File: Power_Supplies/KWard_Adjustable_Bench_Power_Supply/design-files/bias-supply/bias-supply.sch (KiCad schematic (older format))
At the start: 23 parts, among them J1 168VAC input, J2 To C- meter, J3 To panel jacks, Q1 MJE5731, Q2 MJE5731, Q3 KSA1013

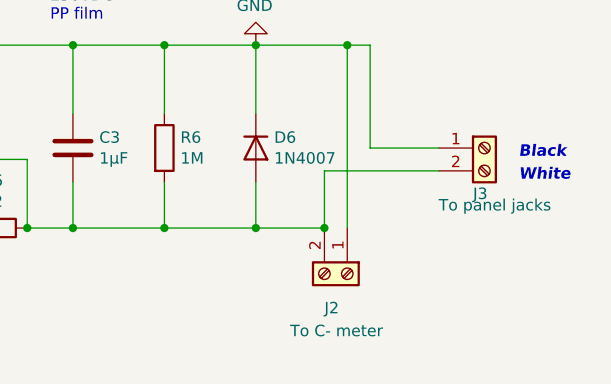
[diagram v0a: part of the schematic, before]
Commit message: Make the C- meter terminal a 3-position part, with a separate one for the GND reference.
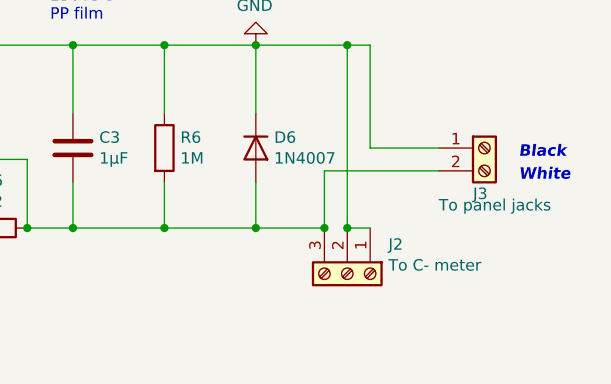
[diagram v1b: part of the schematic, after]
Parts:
- removed J2: To C- meter, TerminalBlock:TerminalBlock_bornier-2_P5.08mm, symbol Connector:Screw_Terminal_01x02
- added J2: To C- meter, TerminalBlock:TerminalBlock_bornier-3_P5.08mm, symbol Connector:Screw_Terminal_01x03
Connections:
- net GND: now also J2.1 (Pin_1), J2.2 (Pin_2)
- net at C3.2, D5.1 (K), D6.2 (A)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: now also J2.3 (Pin_3)
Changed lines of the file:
@@
 $EndComp
 Connection ~ 8200 3450
-$Comp
-L Connector:Screw_Terminal_01x02 J2
-U 1 1 64258EEA
-P 8600 4450
-F 0 "J2" V 8750 4350 50  0000 L CNN
-F 1 "To C- meter" V 8850 4200 50  0000 L CNN
-F 2 "TerminalBlock:TerminalBlock_bornier-2_P5.08mm" H 8600 4450 50  0001 C CNN
-F 3 "~" H 8600 4450 50  0001 C CNN
-	1    8600 4450
-	0    1    1    0
-$EndComp
 Wire Wire Line
 	8500 4250 8200 4250
@@
 Connection ~ 6100 3350
 Connection ~ 7400 3450
+$Comp
+L Connector:Screw_Terminal_01x03 J2
+U 1 1 61D5CFA2
+P 8600 4450
+F 0 "J2" V 8472 4630 50  0000 L CNN
+F 1 "To C- meter" V 8563 4630 50  0000 L CNN
+F 2 "TerminalBlock:TerminalBlock_bornier-3_P5.08mm" H 8600 4450 50  0001 C CNN
+F 3 "~" H 8600 4450 50  0001 C CNN
+	1    8600 4450
+	0    1    1    0
+$EndComp
+Wire Wire Line
+	8700 4250 8600 4250
+Connection ~ 8600 4250
 $EndSCHEMATC

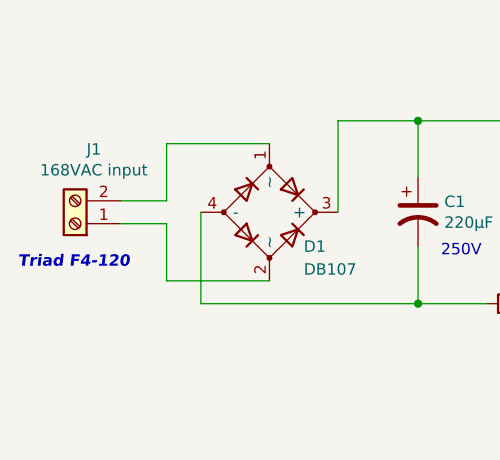
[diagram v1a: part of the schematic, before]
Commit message: Note that the bias supply is connected to the Main 120Vac.
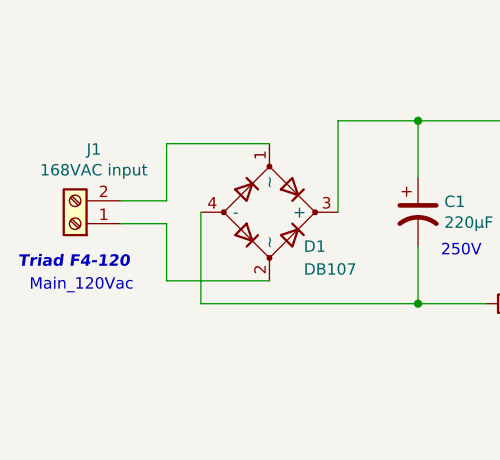
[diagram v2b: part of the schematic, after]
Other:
- note added: "Main_120Vac"
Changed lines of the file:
@@
 	8700 4250 8600 4250
 Connection ~ 8600 4250
+Text Notes 1550 4200 0    50   ~ 0
+Main_120Vac
 $EndSCHEMATC

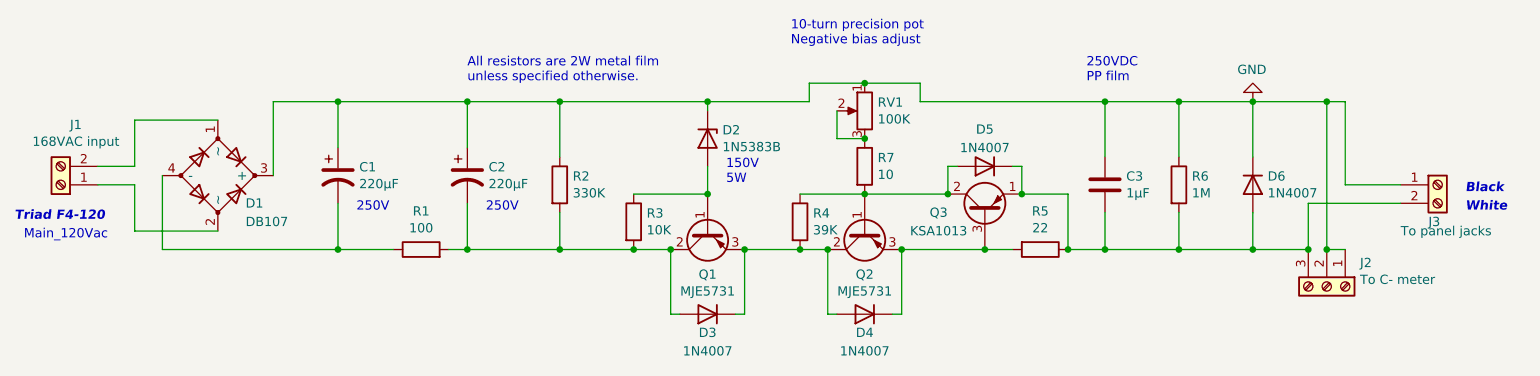
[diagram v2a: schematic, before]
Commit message: Correct AC input value label, add some part numbers, tweak some text.
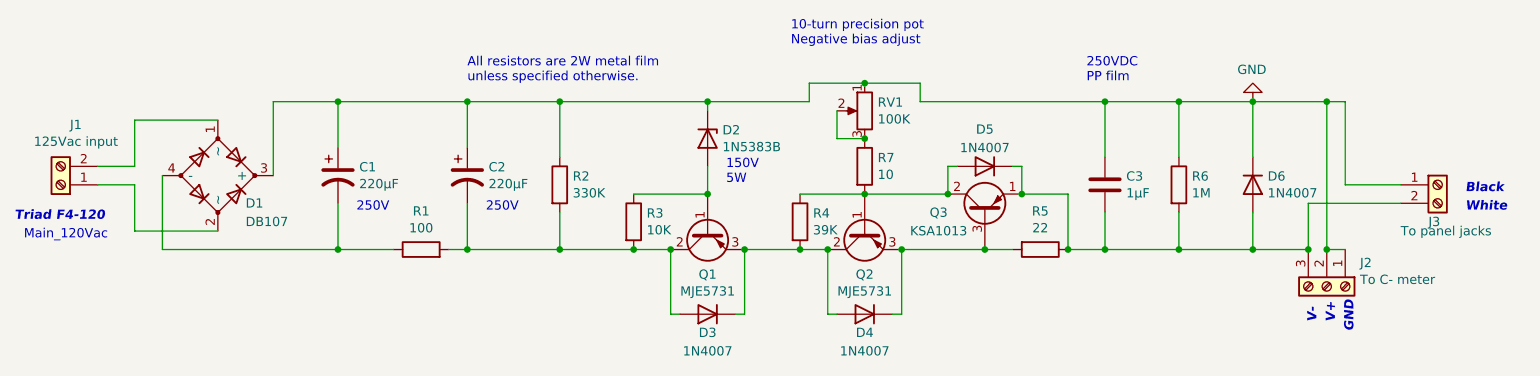
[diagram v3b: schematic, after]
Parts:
- D2: Mouser (none) -> 863-1N5383BG
- D6: Mouser (none) -> 621-1N4007G-T
- J1: value 168VAC input -> 125Vac input
- Q1, Q2: Mouser (none) -> 863-MJE5731G
- Q3: Mouser (none) -> 512-KSA1013YBU
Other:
- note added: "GND"
- note added: "V+"
- note added: "V-"
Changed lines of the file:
@@
 Sheet 1 1
 Title "KWard Bench PSU - Bias supply"
-Date ""
-Rev "0.1"
-Comp "Copyright (c) 2021 Jason R. Thorpe. See LICENSE."
+Date "2022-01-01"
+Rev "1.0"
+Comp "Copyright (c) 2017-2022 Kevin Ward and Jason R. Thorpe. See LICENSE."
 Comment1 ""
 Comment2 ""
@@
 P 1750 3900
 F 0 "J1" H 1668 3575 50  0000 C CNN
-F 1 "168VAC input" H 1668 3666 50  0000 C CNN
+F 1 "125Vac input" H 1668 3666 50  0000 C CNN
 F 2 "TerminalBlock:TerminalBlock_bornier-2_P5.08mm" H 1750 3900 50  0001 C CNN
 F 3 "~" H 1750 3900 50  0001 C CNN
@@
 F 2 "Diode_THT:D_DO-201_P15.24mm_Horizontal" H 5250 3475 50  0001 C CNN
 F 3 "https://diotec.com/tl_files/diotec/files/pdf/datasheets/1n5345b.pdf" H 5250 3650 50  0001 C CNN
+F 4 "863-1N5383BG" V 5250 3650 50  0001 C CNN "Mouser"
 	1    5250 3650
 	0    1    1    0
@@
 F 2 "Package_TO_SOT_THT:TO-220-3_Vertical" H 5450 4250 50  0001 C CNN
 F 3 "~" H 5250 4150 50  0001 C CNN
+F 4 "863-MJE5731G" V 5250 4150 50  0001 C CNN "Mouser"
 	1    5250 4150
 	0    -1   1    0
@@
 F 2 "Package_TO_SOT_THT:TO-220-3_Vertical" H 6300 4250 50  0001 C CNN
 F 3 "~" H 6100 4150 50  0001 C CNN
+F 4 "863-MJE5731G" V 6100 4150 50  0001 C CNN "Mouser"
 	1    6100 4150
 	0    -1   1    0
@@
 F 2 "Package_TO_SOT_THT:TO-92L" H 6950 4150 50  0001 C CNN
 F 3 "~" H 6750 4050 50  0001 C CNN
+F 4 "512-KSA1013YBU" V 6750 4050 50  0001 C CNN "Mouser"
 	1    6750 4050
 	0    -1   -1   0
@@
 F 2 "Diode_THT:D_DO-41_SOD81_P10.16mm_Horizontal" H 8200 3725 50  0001 C CNN
 F 3 "http://www.vishay.com/docs/88503/1n4001.pdf" H 8200 3900 50  0001 C CNN
+F 4 "621-1N4007G-T" V 8200 3900 50  0001 C CNN "Mouser"
 	1    8200 3900
 	0    1    1    0
@@
 Text Notes 1550 4200 0    50   ~ 0
 Main_120Vac
+Text Notes 8550 4650 1    50   Italic 10
+V-
+Text Notes 8650 4650 1    50   Italic 10
+V+
+Text Notes 8750 4700 1    50   Italic 10
+GND
 $EndSCHEMATC
